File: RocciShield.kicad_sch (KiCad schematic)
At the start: 176 parts, among them J1 Battery, J10 M3, J11 I2C6, J12 M4, J13 I2C7, J14 Power, J2 I2C0, J3 I2C1, J4 I2C2, J5 I2C3, J6 M1, J7 I2C4, J8 M2, J9 I2C5, Q1 IRF7416, U1 LMR33630, U2 AMS1117-3.3, U3 L7808, U4 TPS3700, U5 TCA9548A, U6 DRV8871, U7 DRV8871, U8 DRV8871, U9 DRV8871

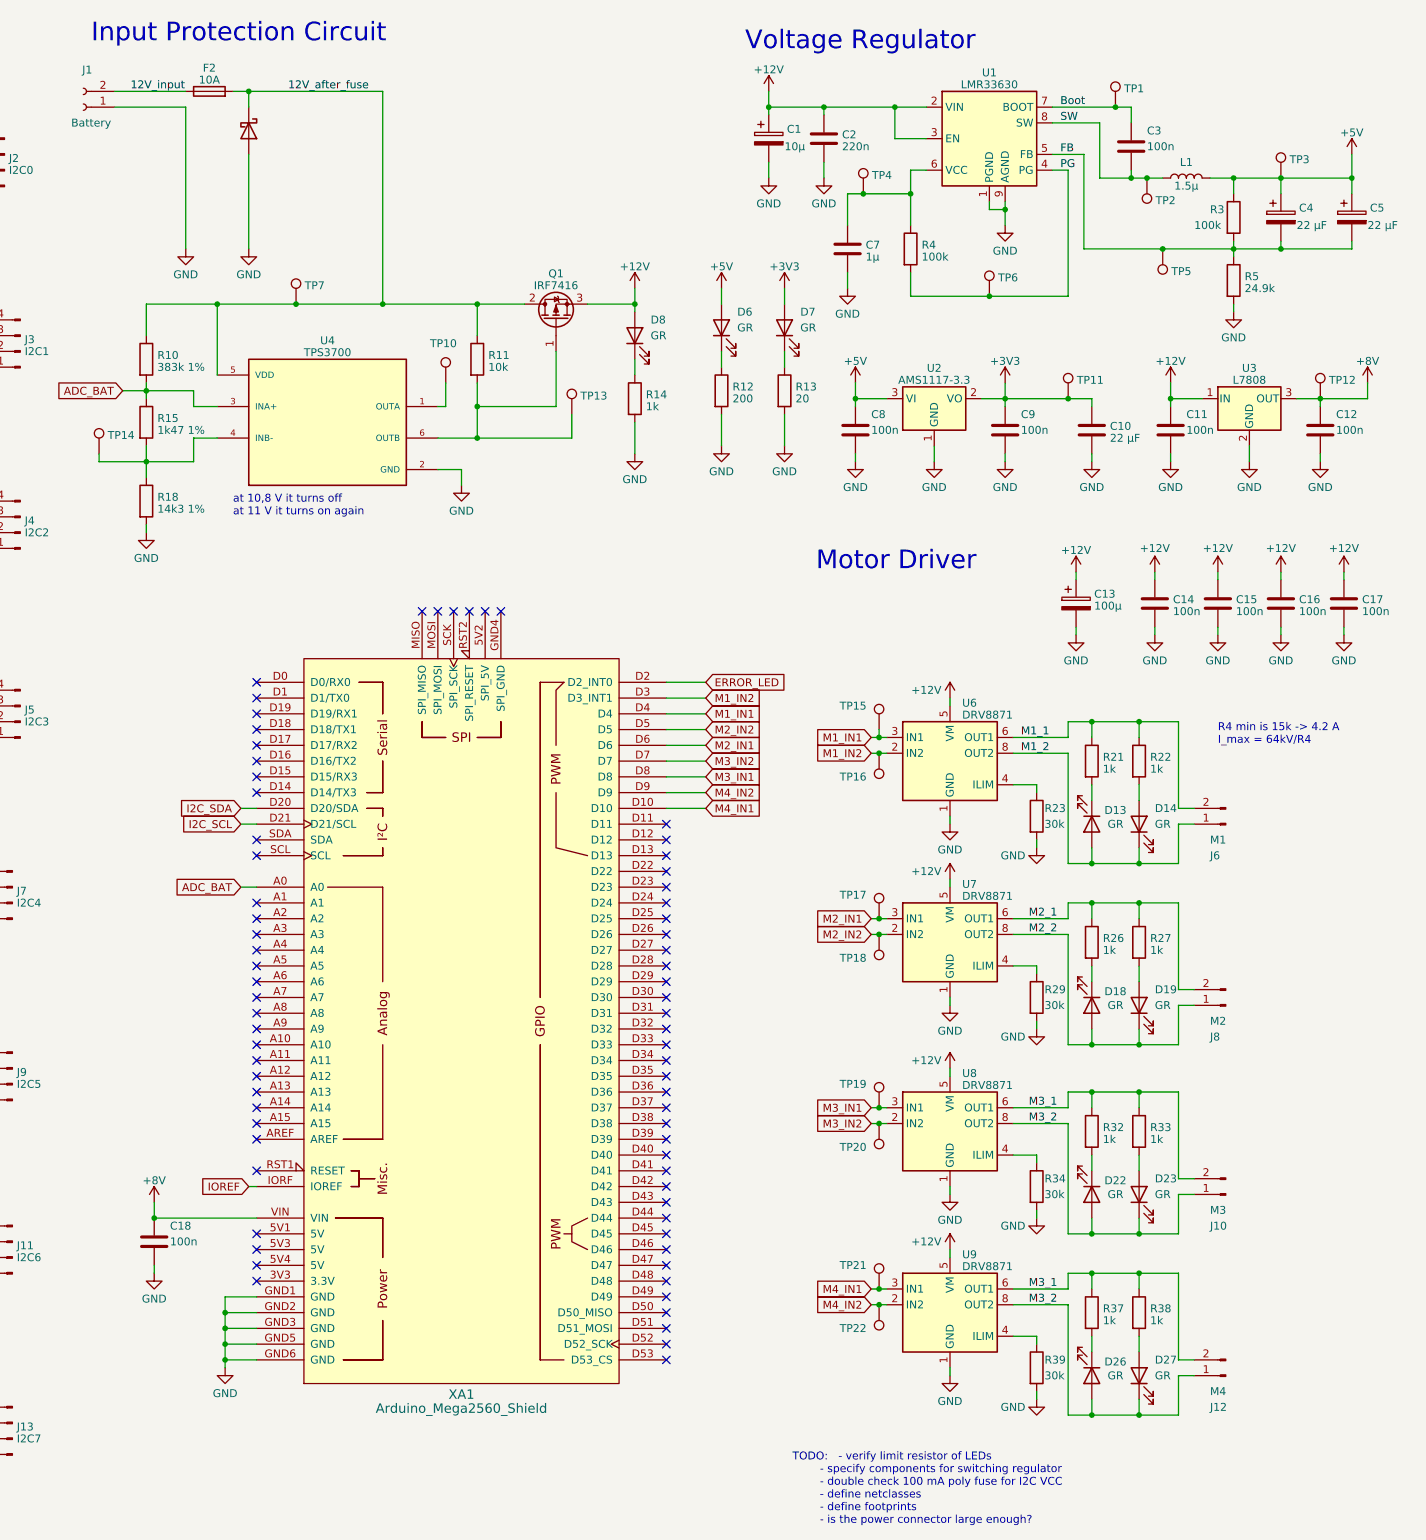
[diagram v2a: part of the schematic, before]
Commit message: changed pwm pins, added footprints, started JLPCB component selection
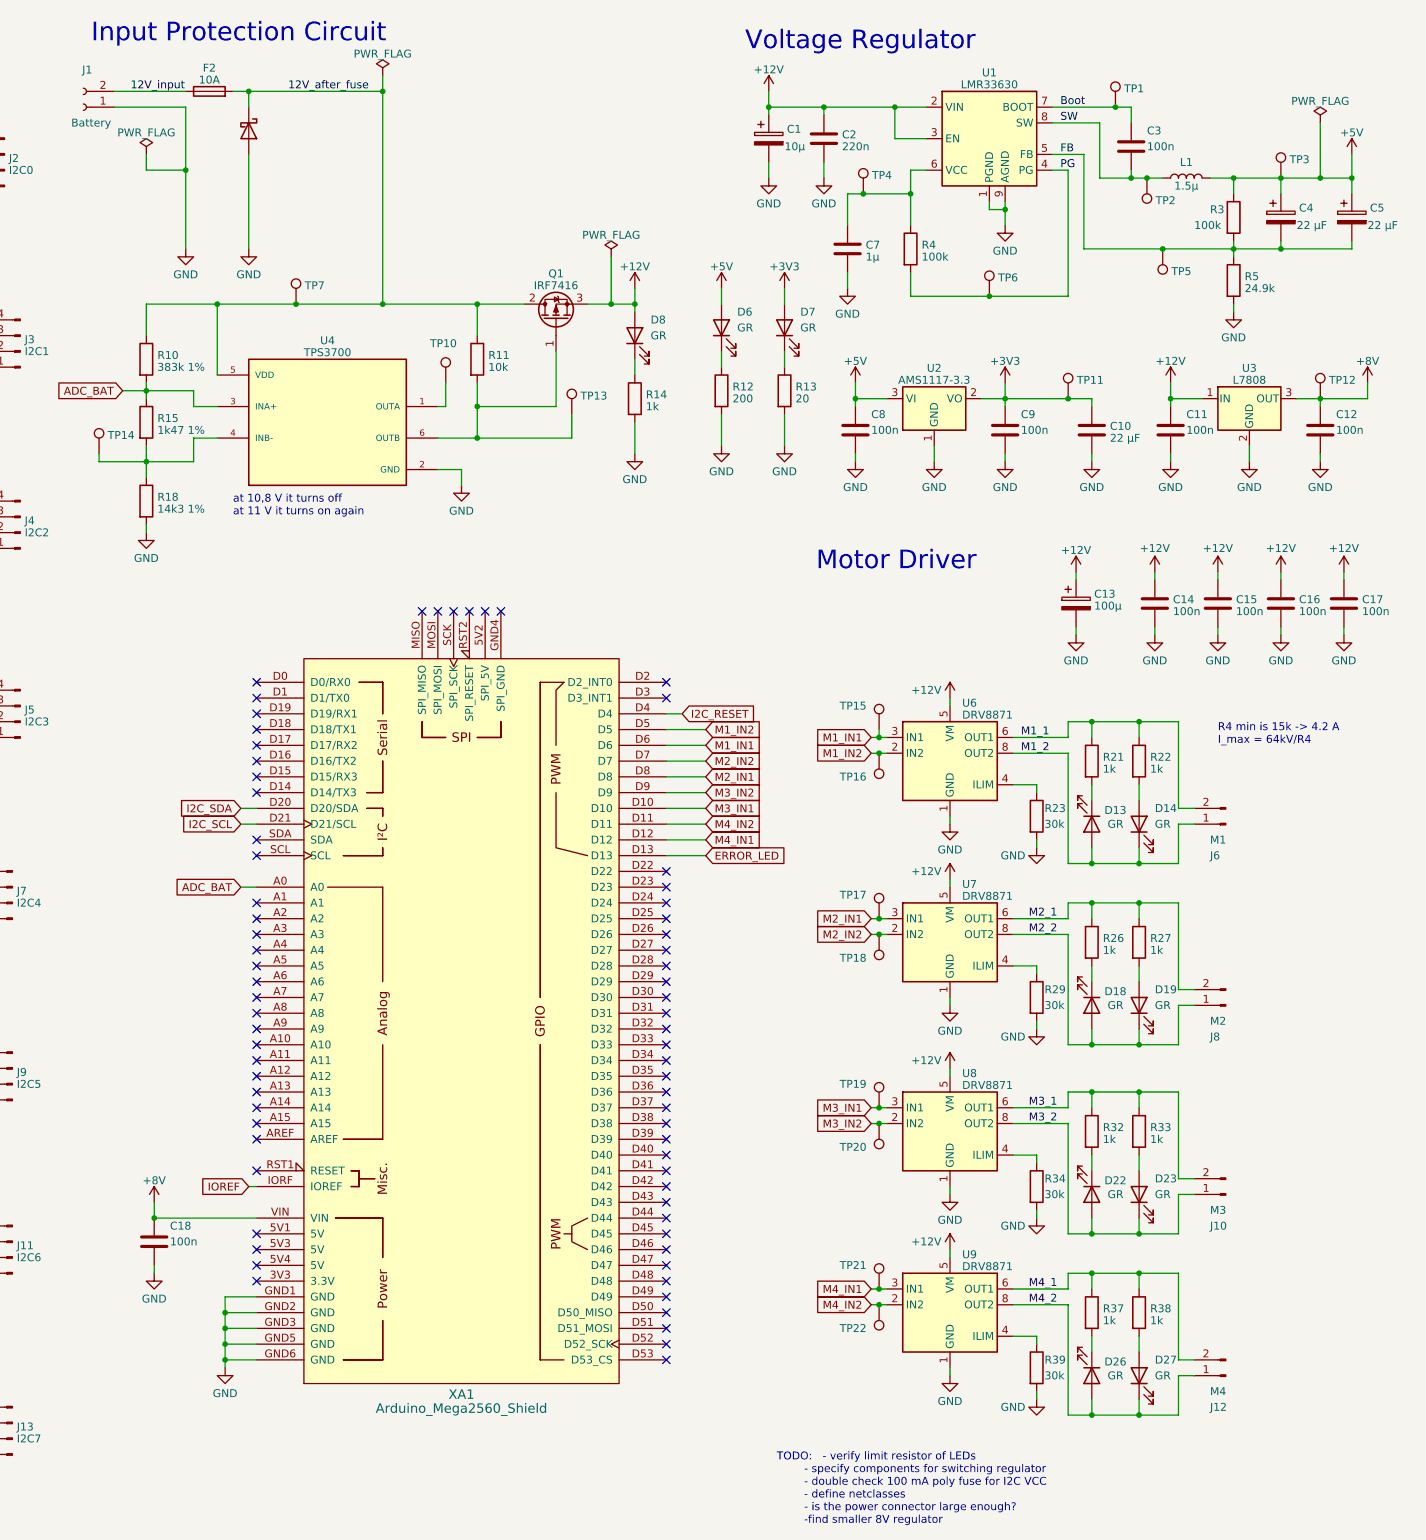
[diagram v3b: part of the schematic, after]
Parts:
- C1, C10, C4, C5, C7: footprint (none) -> Capacitor_SMD:CP_Elec_5x3
- C11, C12, C13, C14, C15, C16, C17, C18, C2, C3, C6, C8, C9: footprint (none) -> Capacitor_SMD:C_0603_1608Metric
- D1, D10, D11, D12, D15, D16, D2, D20, D21, D24, D25, D28, D29, D4, D5, D9: footprint Diode_THT:D_DO-35_SOD27_P7.62mm_Horizontal -> Diode_SMD:D_SOD-123
- D13, D14, D17, D18, D19, D22, D23, D26, D27, D30, D31, D6, D7, D8: footprint (none) -> LED_SMD:LED_0603_1608Metric
- F1, F10, F11, F12, F13, F14, F15, F16, F17, F18, F19, F2, F20, F21, F22, F23, F24, F25, F3, F4, F5, F6, F7, F8, F9: footprint (none) -> Fuse:Fuse_0805_2012Metric
- F26, F27: footprint (none) -> Fuse:Fuse_1812_4532Metric
- J1: footprint (none) -> Connector_AMASS:AMASS_XT30U-M_1x02_P5.0mm_Vertical
- J10, J12, J6, J8: footprint (none) -> Connector_PinHeader_2.54mm:PinHeader_1x02_P2.54mm_Vertical
- J11, J13, J14, J2, J3, J4, J5, J7, J9: footprint (none) -> Connector_PinHeader_2.54mm:PinHeader_1x04_P2.54mm_Vertical
- JP1, JP10, JP11, JP2, JP3, JP4, JP5, JP6, JP7, JP8, JP9: footprint (none) -> Jumper:SolderJumper-3_P1.3mm_Open_Pad1.0x1.5mm
- L1: footprint (none) -> Inductor_SMD:L_6.3x6.3_H3
- Q1: footprint (none) -> Package_SO:SO-8_5.3x6.2mm_P1.27mm
- R1, R10, R11, R12, R13, R14, R15, R16, R17, R18, R19, R2, R20, R21, R22, R23, R24, R25, R26, R27, R28, R29, R3, R30, R31, R32, R33, R34, R35, R36, R37, R38, R39, R4, R40, R41, R5, R6, R7, R8, R9: footprint (none) -> Resistor_SMD:R_0603_1608Metric
- TP1, TP10, TP11, TP12, TP13, TP14, TP15, TP16, TP17, TP18, TP19, TP2, TP20, TP21, TP22, TP3, TP4, TP5, TP6, TP7, TP8, TP9: footprint (none) -> TestPoint:TestPoint_Pad_D1.0mm
- U3: footprint (none) -> Package_TO_SOT_SMD:SOT-223-3_TabPin2
- U4: footprint SOT95P280X110-6N -> Package_TO_SOT_SMD:SOT-23-6
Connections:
- net ERROR_LED: now also XA1.D13; no longer XA1.D2 (D2_INT0)
- net I2C_RESET: now also XA1.D4
- net M1_IN1: now also XA1.D6; no longer XA1.D4
- net M1_IN2: now also XA1.D5; no longer XA1.D3 (D3_INT1)
- net M2_IN1: now also XA1.D8; no longer XA1.D6
- net M2_IN2: now also XA1.D7; no longer XA1.D5
- net M3_1: no longer J12.2 (Pin_2), R37.1, R38.1, U9.6 (OUT1)
- net M3_2: no longer D26.2 (A), D27.1 (K), J12.1 (Pin_1), U9.8 (OUT2)
- net M3_IN1: now also XA1.D10; no longer XA1.D8
- net M3_IN2: now also XA1.D9; no longer XA1.D7
- net M4_IN1: now also XA1.D12; no longer XA1.D10
- net M4_IN2: now also XA1.D11; no longer XA1.D9
- new net M4_1: J12.2 (Pin_2), R37.1, R38.1, U9.6 (OUT1)
- new net M4_2: D26.2 (A), D27.1 (K), J12.1 (Pin_1), U9.8 (OUT2)
- no-connect marks 72 -> 71
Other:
- note added: "TODO: - verify limit resistor of LEDs - specify components for switching regulator - double check 100 mA poly fuse for I2C VCC - define netclasses - is the power connector large enough? -find smaller 8V regulator"
- note removed: "TODO: - verify limit resistor of LEDs - specify components for switching regulator - double check 100 mA poly fuse for I2C VCC - define netclasses - define footprints - is the power connector large enough?"
